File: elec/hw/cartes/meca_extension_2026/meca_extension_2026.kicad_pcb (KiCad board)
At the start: 4 copper layers, 126.2 x 84.5 mm, 194 parts, among them J1 2-1445051-3, J10 22053051, J11 B2B-XH-A, J12 22272021, J13 22053051, J14 22272031, J15 22272031, J16 5264-3P, J17 5267-3P, J18 5267-3P, J19 5267-3P, J2 B2B-XH-A, J20 5267-3P, J24 22053031, J25 22053031, J26 22053051, J27 22053041, J28 22053031, J29 22053031, J3 22272021, J4 22053051, J5 B2B-XH-A, J6 22272021, J7 22053051, J8 B2B-XH-A, J9 22272021, Q1 SI2310, Q10 SI2310, Q11 SI2310, Q12 2N7002, Q13 2N7002, Q14 2N7002, Q19 BSS84, Q2 SI2310, Q20 2N7002, Q3 2N7002, Q4 SI2310, Q5 SI2310, Q6 2N7002, Q7 SI2310, Q8 SI2310, Q9 2N7002, U1 TCA9548APWR, U11 LV14340DDAR, U2 PCA9535PW, U3 TLA2528IRTER, U4 TLV9061IDBVR, U5 TLV9061IDBVR, U6 TLV9061IDBVR, U7 TLV9061IDBVR, U8 74HCT238PW, U9 SN74LVC1T45DBV

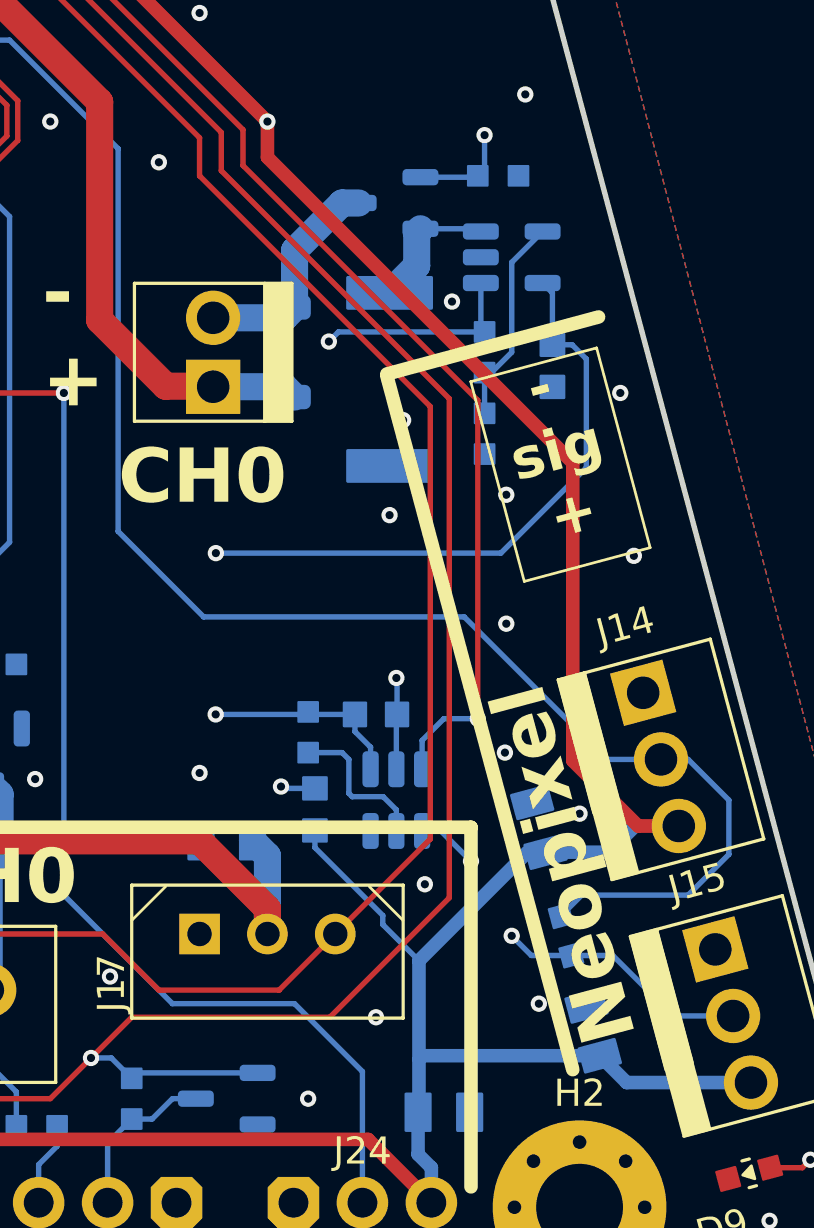
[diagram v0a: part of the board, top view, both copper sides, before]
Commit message: meca_extension : led command can be 3v3 or 5v, selecion resistors added
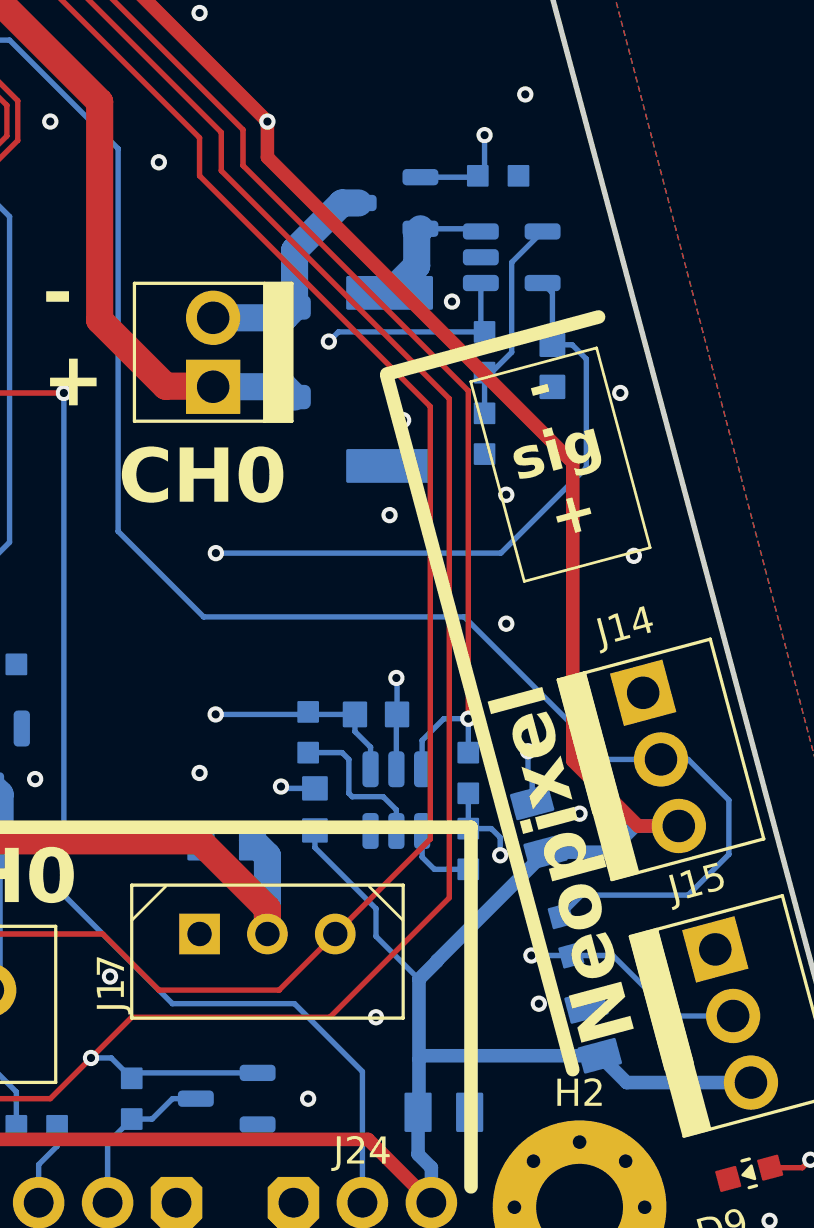
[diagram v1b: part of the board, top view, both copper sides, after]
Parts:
- added R65: 0R, cocotter_resistor:r0603_reflow, B.Cu at (174.4, 113.8)
- added R66: 0R, cocotter_resistor:r0603_reflow, B.Cu at (174.4, 111.0)
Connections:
- net /neopixel_cmd_3v3 renamed /neopixel_cmd_con
- U9 pad 4: /neopixel_cmd_5v -> Net-(U9-B)
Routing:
- net Net-(U9-B): track 0.00 -> 2.85 mm
- net GND: track 10.8 -> 12.8 mm, vias 141 -> 140
- net /neopixel_cmd_5v: track 15.0 -> 15.8 mm
- net /neopixel_cmd_con: track 93.1 -> 93.9 mm
